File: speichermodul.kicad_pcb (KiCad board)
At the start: 2 copper layers, 100 x 160 mm, 66 parts, among them IC1 6116, P1 CONN_3X2, P2 CONN_01X01, P3 CONN_01X01, P4 CONN_01X01, P5 CONN_01X01, P6 CONN_01X01, P7 CONN_01X01, P8 CONN_02X10, P9 CONN_02X10, SW1 SW_PUSH, SW2 SW_PUSH, U1 7400, U2 74LS08, U3 74LS08, U4 74LS14, U5 74LS540, U6 74LS540

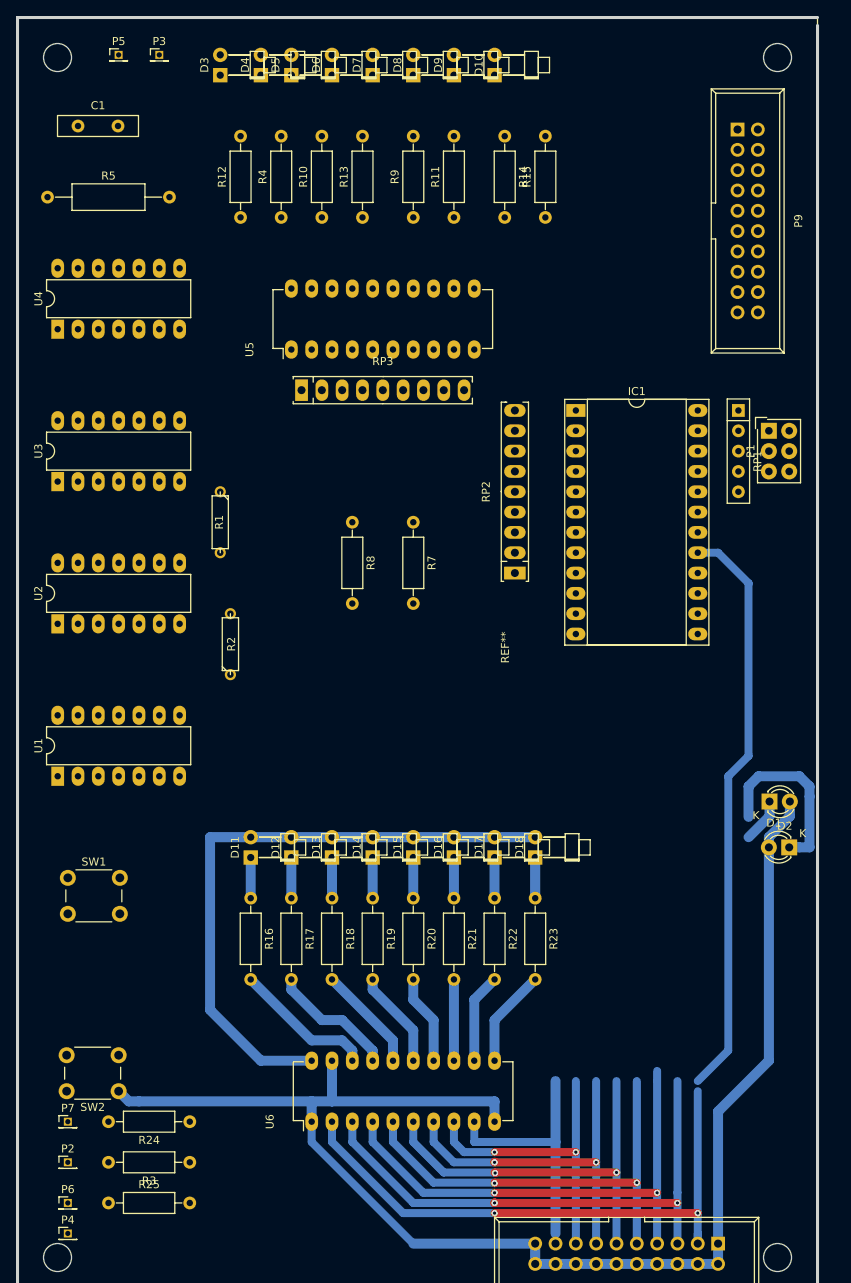
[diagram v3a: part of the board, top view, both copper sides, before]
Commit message: PCB layout revolutioniert
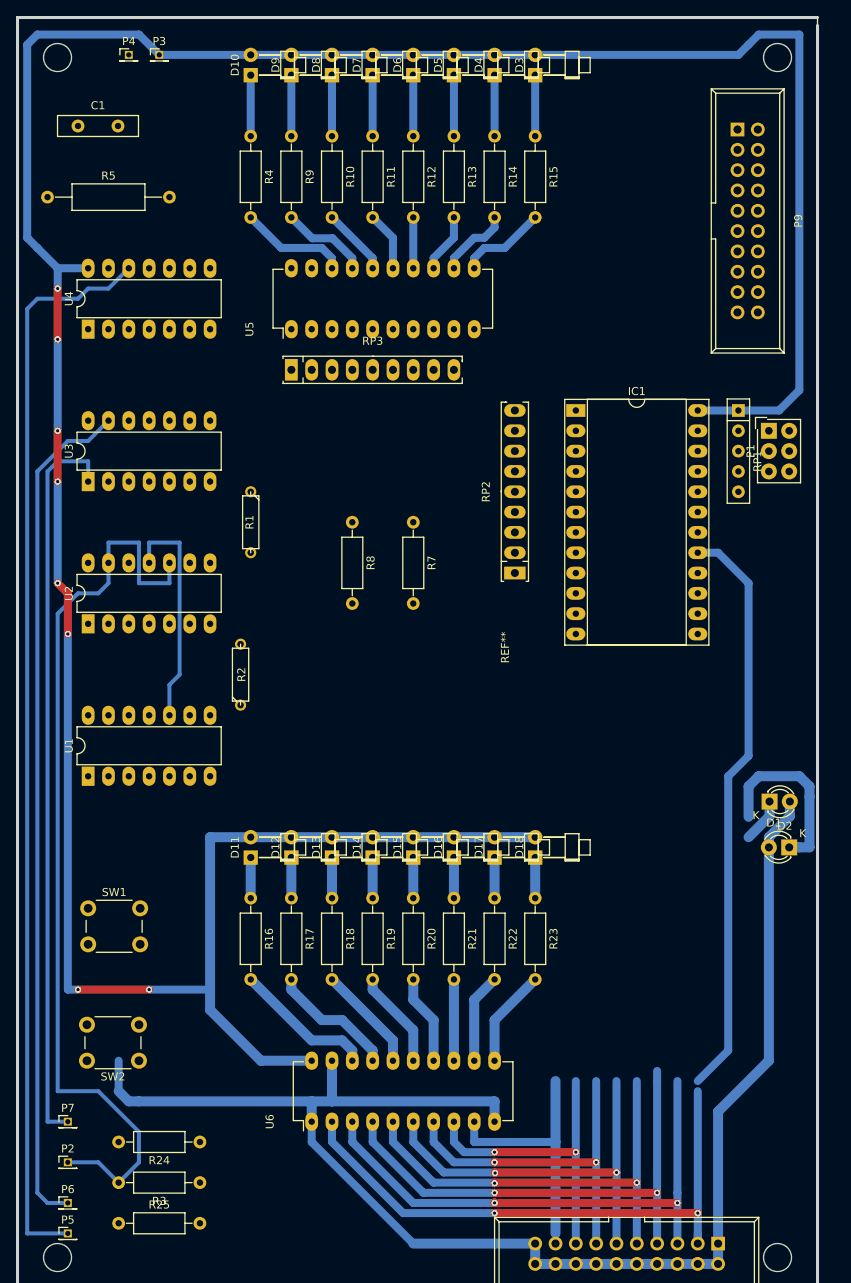
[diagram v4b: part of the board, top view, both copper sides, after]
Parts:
- moved P4 147.5 mm to (41.9, 26.7)
- moved P5 147.5 mm to (34.3, 174.0)
- moved D3 39.4 mm to (92.7, 29.2)
- moved D10 30.5 mm to (57.1, 29.2)
- moved D4 29.2 mm to (87.6, 29.2)
- moved R12 23.9 mm to (77.5, 36.8), turned to 270 degrees
- moved D5 20.3 mm to (82.5, 29.2)
- moved D9 20.3 mm to (62.2, 29.2)
- moved R9 18.3 mm to (62.2, 36.8), turned to 270 degrees
- moved R13 15.3 mm to (82.5, 36.8), turned to 270 degrees
- moved R11 14.4 mm to (72.4, 36.8), turned to 270 degrees
- moved R4 10.9 mm to (57.1, 36.8), turned to 270 degrees
- moved R15 10.2 mm to (92.7, 36.8), turned to 270 degrees
- moved R10 10.2 mm to (67.3, 36.8), turned to 270 degrees
- moved D6 10.2 mm to (77.5, 29.2)
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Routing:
- net VCC: track 77.6 -> 376.7 mm, vias 0 -> 8
- net Net-(P5-Pad1): track 0.00 -> 135.5 mm
- net /_auto: track 0.00 -> 115.0 mm
- net Net-(P6-Pad1): track 0.00 -> 106.0 mm
- net Net-(P7-Pad1): track 0.00 -> 92.0 mm
- net Net-(U1-Pad10): track 0.00 -> 28.5 mm
- net Net-(R4-Pad2): track 0.00 -> 13.5 mm
- net Net-(R9-Pad2): track 0.00 -> 11.0 mm
- net Net-(R15-Pad2): track 0.00 -> 11.0 mm
- net Net-(R14-Pad2): track 0.00 -> 9.20 mm
- net Net-(R10-Pad2): track 0.00 -> 8.45 mm
- net Net-(D9-Pad1): track 0.00 -> 7.62 mm
- net Net-(D8-Pad1): track 0.00 -> 7.62 mm
- net Net-(D7-Pad1): track 0.00 -> 7.62 mm
- net Net-(D6-Pad1): track 0.00 -> 7.62 mm
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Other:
- net class Default: trace_width 1 -> 0.5

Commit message: minimal änderungen
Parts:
- moved P8 139.7 mm to (118.1, 35.6), turned to 270 degrees
- moved P9 139.3 mm to (115.6, 175.3), turned to 180 degrees
- moved SW2 16.6 mm to (44.5, 135.9)
- moved SW1 15.2 mm to (36.8, 148.6)
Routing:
- net GND: track 184.1 -> 103.5 mm
- net /D7: track 72.8 -> 0.00 mm
- net Net-(U1-Pad5): track 0.00 -> 18.1 mm
- net /A2: track 62.3 -> 47.1 mm
- net /A1: track 66.8 -> 51.6 mm
- net /A0: track 72.3 -> 57.0 mm
- net /A3: track 55.5 -> 42.8 mm
- net /A4: track 49.9 -> 38.5 mm
- net VCC: track 376.7 -> 386.9 mm
- net /A5: track 44.4 -> 34.2 mm
- net /A6: track 38.6 -> 29.7 mm
- net Net-(U2-Pad6): track 0.00 -> 7.62 mm
- net Net-(U2-Pad12): track 0.00 -> 7.62 mm
- net /A7: track 31.8 -> 25.4 mm

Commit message: Nix
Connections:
- P9 pad 11: /D4 -> /D3
- P9 pad 13: /D5 -> /D2
- P9 pad 15: /D6 -> /D1
- P9 pad 17: /D7 -> /D0
- P9 pad 3: /D0 -> /D7
- P9 pad 5: /D1 -> /D6
- P9 pad 7: /D2 -> /D5
- P9 pad 9: /D3 -> /D4
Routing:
- net /A0: track 57.0 -> 26.5 mm, vias 2 -> 1
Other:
- net class Default: trace_width 0.5 -> 0.9
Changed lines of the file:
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@@
-(kicad_pcb (version 20171130) (host pcbnew no-vcs-found-bf44d39~61~ubuntu16.04.1)
+(kicad_pcb (version 20171130) (host pcbnew 5.0.0-rc2-dev-unknown-41ac458~64~ubuntu16.04.1)
   (general
     (thickness 1.6)
     (drawings 0)
-    (tracks 244)
+    (tracks 240)
     (zones 0)
     (modules 66)
@@
   )
   (setup
-    (last_trace_width 0.5)
+    (last_trace_width 0.9)
     (trace_clearance 0.2)
     (zone_clearance 0.508)
@@
   (net_class Default "This is the default net class."
     (clearance 0.2)
-    (trace_width 0.5)
+    (trace_width 0.9)
     (via_dia 0.8)
     (via_drill 0.4)
@@
       (net 10 GND))
     (pad 3 thru_hole oval (at 2.54 0 180) (size 1.7272 1.7272) (drill 1.016) (layers *.Cu *.Mask F.SilkS)
-      (net 2 /D0))
+      (net 9 /D7))
     (pad 4 thru_hole oval (at 2.54 -2.54 180) (size 1.7272 1.7272) (drill 1.016) (layers *.Cu *.Mask F.SilkS)
       (net 10 GND))
     (pad 5 thru_hole oval (at 5.08 0 180) (size 1.7272 1.7272) (drill 1.016) (layers *.Cu *.Mask F.SilkS)
-      (net 3 /D1))
+      (net 8 /D6))
     (pad 6 thru_hole oval (at 5.08 -2.54 180) (size 1.7272 1.7272) (drill 1.016) (layers *.Cu *.Mask F.SilkS)
       (net 10 GND))
     (pad 7 thru_hole oval (at 7.62 0 180) (size 1.7272 1.7272) (drill 1.016) (layers *.Cu *.Mask F.SilkS)
-      (net 4 /D2))
+      (net 7 /D5))
     (pad 8 thru_hole oval (at 7.62 -2.54 180) (size 1.7272 1.7272) (drill 1.016) (layers *.Cu *.Mask F.SilkS)
       (net 10 GND))
     (pad 9 thru_hole oval (at 10.16 0 180) (size 1.7272 1.7272) (drill 1.016) (layers *.Cu *.Mask F.SilkS)
-      (net 5 /D3))
+      (net 6 /D4))
     (pad 10 thru_hole oval (at 10.16 -2.54 180) (size 1.7272 1.7272) (drill 1.016) (layers *.Cu *.Mask F.SilkS)
       (net 10 GND))
     (pad 11 thru_hole oval (at 12.7 0 180) (size 1.7272 1.7272) (drill 1.016) (layers *.Cu *.Mask F.SilkS)
-      (net 6 /D4))
+      (net 5 /D3))
     (pad 12 thru_hole oval (at 12.7 -2.54 180) (size 1.7272 1.7272) (drill 1.016) (layers *.Cu *.Mask F.SilkS)
       (net 10 GND))
     (pad 13 thru_hole oval (at 15.24 0 180) (size 1.7272 1.7272) (drill 1.016) (layers *.Cu *.Mask F.SilkS)
-      (net 7 /D5))
+      (net 4 /D2))
     (pad 14 thru_hole oval (at 15.24 -2.54 180) (size 1.7272 1.7272) (drill 1.016) (layers *.Cu *.Mask F.SilkS)
       (net 10 GND))
     (pad 15 thru_hole oval (at 17.78 0 180) (size 1.7272 1.7272) (drill 1.016) (layers *.Cu *.Mask F.SilkS)
-      (net 8 /D6))
+      (net 3 /D1))
     (pad 16 thru_hole oval (at 17.78 -2.54 180) (size 1.7272 1.7272) (drill 1.016) (layers *.Cu *.Mask F.SilkS)
       (net 10 GND))
     (pad 17 thru_hole oval (at 20.32 0 180) (size 1.7272 1.7272) (drill 1.016) (layers *.Cu *.Mask F.SilkS)
-      (net 9 /D7))
+      (net 2 /D0))
     (pad 18 thru_hole oval (at 20.32 -2.54 180) (size 1.7272 1.7272) (drill 1.016) (layers *.Cu *.Mask F.SilkS)
       (net 10 GND))
@@
   (segment (start 69.85 162.56) (end 77.47 170.18) (width 1) (layer B.Cu) (net 33))
   (segment (start 87.63 170.18) (end 87.63 170.18) (width 1) (layer F.Cu) (net 33) (status 2))
-  (via (at 113.03 171.45) (size 0.8) (drill 0.4) (layers F.Cu B.Cu) (net 34))
-  (segment (start 67.31 162.56) (end 76.2 171.45) (width 1) (layer B.Cu) (net 34))
-  (segment (start 76.2 171.45) (end 87.63 171.45) (width 1) (layer B.Cu) (net 34))
-  (segment (start 67.31 160.02) (end 67.31 162.56) (width 1) (layer B.Cu) (net 34) (status 400000))
+  (segment (start 67.31 160.02) (end 67.31 162.56) (width 0.9) (layer B.Cu) (net 34))
+  (segment (start 67.31 162.56) (end 76.2 171.45) (width 0.9) (layer B.Cu) (net 34))
   (via (at 87.63 171.45) (size 0.8) (drill 0.4) (layers F.Cu B.Cu) (net 34))
-  (segment (start 87.63 171.45) (end 113.03 171.45) (width 1) (layer F.Cu) (net 34))
-  (segment (start 113.03 175.26) (end 113.03 171.45) (width 1) (layer B.Cu) (net 34) (status 400000))
-  (segment (start 113.03 175.26) (end 113.03 173.99) (width 1) (layer B.Cu) (net 34) (status 400000))
+  (segment (start 76.2 171.45) (end 87.63 171.45) (width 0.9) (layer B.Cu) (net 34))
   (segment (start 124.46 125.73) (end 125.73 125.73) (width 1.25) (layer B.Cu) (net 35) (status 400000))
   (segment (start 119.38 118.11) (end 119.38 121.92) (width 1.25) (layer B.Cu) (net 35))
@@
   (segment (start 62.23 36.83) (end 62.23 29.21) (width 1) (layer B.Cu) (net 68) (status C00000))
   (segment (start 57.15 36.83) (end 57.15 29.21) (width 1) (layer B.Cu) (net 69) (status C00000))
-  (segment (start 57.15 132.08) (end 57.15 127) (width 1.25) (layer B.Cu) (net 77) (status C00000))
-  (segment (start 62.23 132.08) (end 62.23 127) (width 1.25) (layer B.Cu) (net 76) (status C00000))
-  (segment (start 67.31 132.08) (end 67.31 127) (width 1.25) (layer B.Cu) (net 75) (status C00000))
-  (segment (start 72.39 132.08) (end 72.39 127) (width 1.25) (layer B.Cu) (net 74) (status C00000))
-  (segment (start 77.47 132.08) (end 77.47 127) (width 1.25) (layer B.Cu) (net 73) (status C00000))
-  (segment (start 82.55 132.08) (end 82.55 127) (width 1.25) (layer B.Cu) (net 72) (status C00000))
-  (segment (start 87.63 132.08) (end 87.63 127) (width 1.25) (layer B.Cu) (net 71) (status C00000))
   (segment (start 92.71 132.08) (end 92.71 127) (width 1.25) (layer B.Cu) (net 70) (status C00000))
+  (segment (start 87.63 132.08) (end 87.63 127) (width 1.25) (layer B.Cu) (net 71) (status C00000))
+  (segment (start 82.55 132.08) (end 82.55 127) (width 1.25) (layer B.Cu) (net 72) (status C00000))
+  (segment (start 77.47 132.08) (end 77.47 127) (width 1.25) (layer B.Cu) (net 73) (status C00000))
+  (segment (start 72.39 132.08) (end 72.39 127) (width 1.25) (layer B.Cu) (net 74) (status C00000))
+  (segment (start 67.31 132.08) (end 67.31 127) (width 1.25) (layer B.Cu) (net 75) (status C00000))
+  (segment (start 62.23 132.08) (end 62.23 127) (width 1.25) (layer B.Cu) (net 76) (status C00000))
+  (segment (start 57.15 132.08) (end 57.15 127) (width 1.25) (layer B.Cu) (net 77) (status C00000))
 )

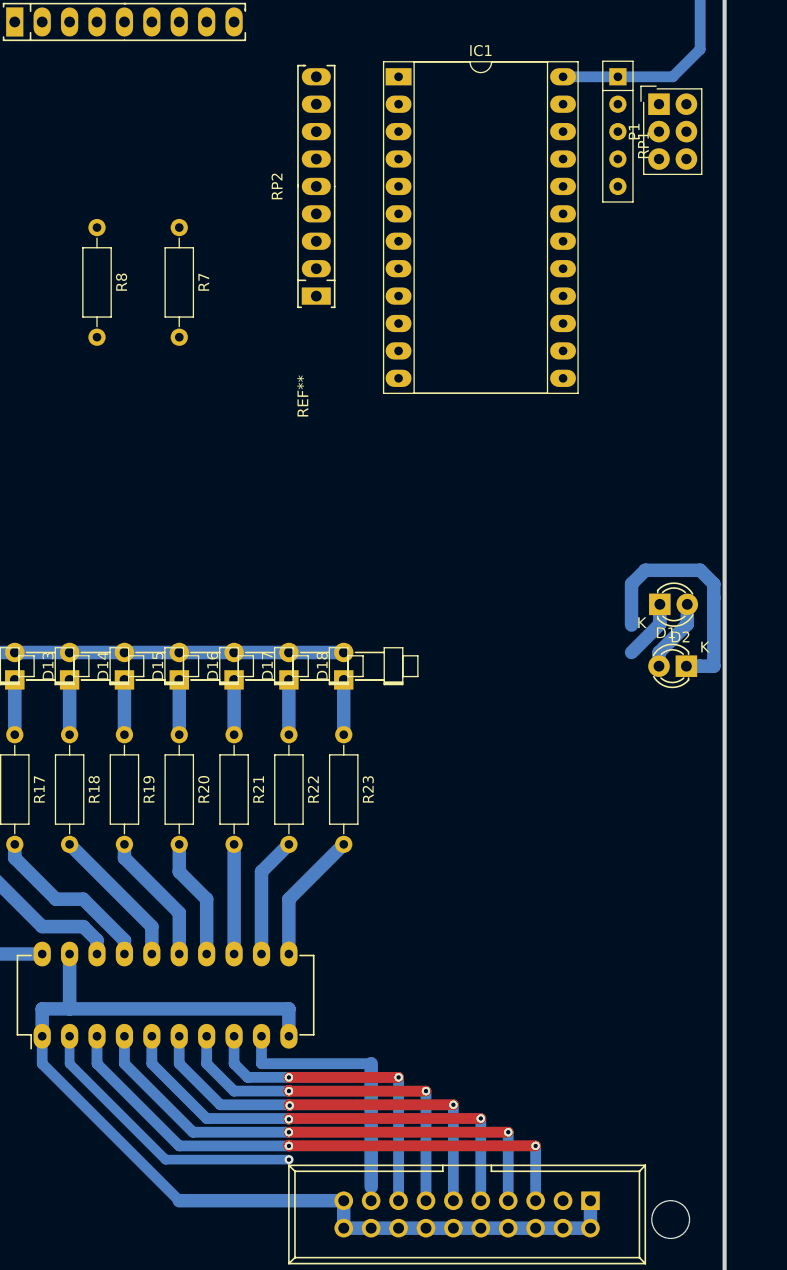
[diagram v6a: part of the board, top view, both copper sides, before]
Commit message: ein einzelnes footprint geändert
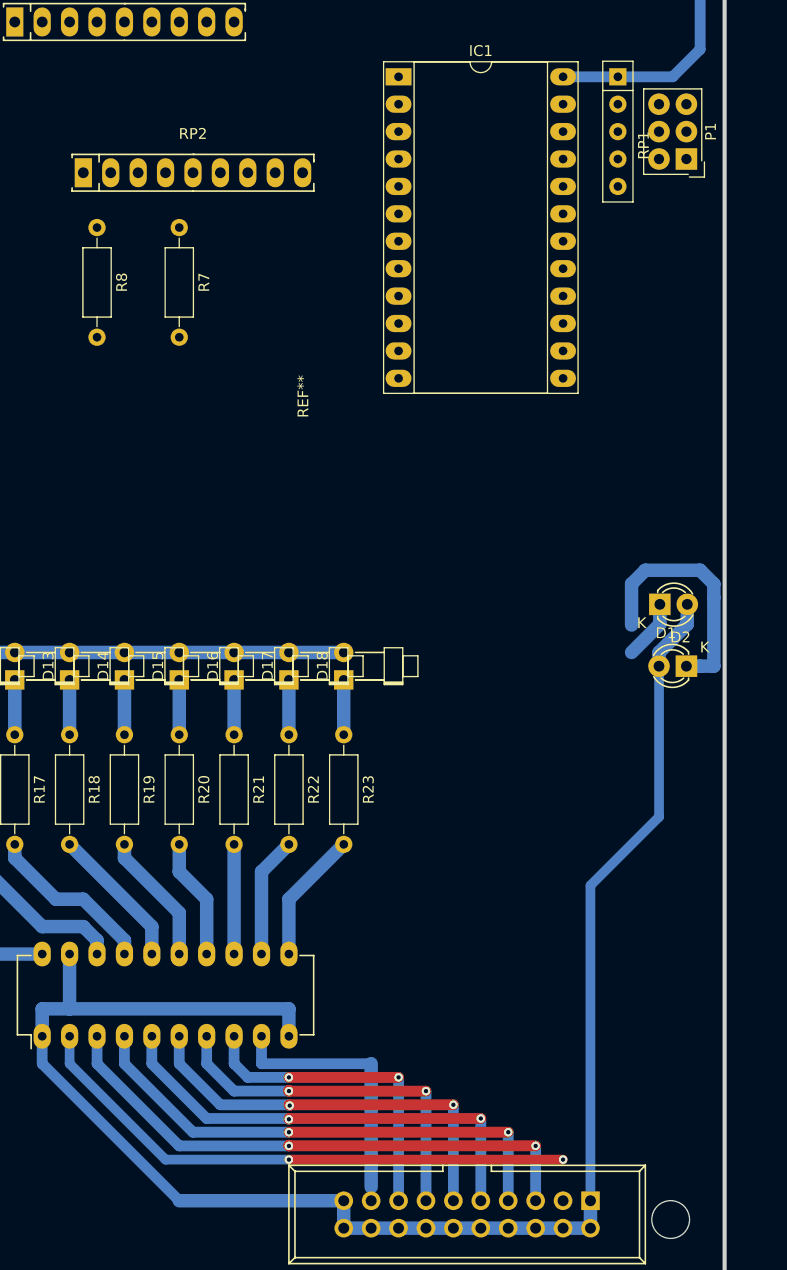
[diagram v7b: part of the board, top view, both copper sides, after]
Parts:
- moved RP2 11.5 mm to (78.7, 80.0), turned to 0 degrees
- moved P1 5.68 mm to (124.5, 78.7), turned to 180 degrees
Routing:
- net GND: track 103.5 -> 155.7 mm
- net /A0: track 26.5 -> 51.9 mm, vias 1 -> 2

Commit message: KAel verlegt
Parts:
- removed the REF** at (28.0, 22.0)
- removed RP2: R_PACK8BUSSED, Housings_SIP:SIP9_Housing_BigPads
- added REF**: EuroBoard160mmX100mm, EuroBoard_Outline:EuroBoard160mmX100mm, F.Cu at (128.3, 181.6)
- moved SW2 17.8 mm to (43.2, 153.7)
- moved SW1 15.2 mm to (36.8, 133.3)
- moved R1 1.27 mm to (58.4, 85.1)
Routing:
- net GND: track 155.7 -> 311.2 mm
- net /D7: track 0.00 -> 93.4 mm
- net /D0: track 0.00 -> 93.0 mm
- net /D6: track 0.00 -> 90.9 mm
- net /D1: track 0.00 -> 89.4 mm
- net /D5: track 0.00 -> 88.3 mm
- net /D4: track 0.00 -> 85.8 mm
- net /D2: track 0.00 -> 85.8 mm
- net /D3: track 0.00 -> 83.3 mm
- net VCC: track 386.9 -> 463.0 mm
- net /A0: track 51.9 -> 0.00 mm, vias 2 -> 0
- net /A1: track 51.6 -> 0.00 mm, vias 2 -> 0
- net /A2: track 47.1 -> 0.00 mm, vias 2 -> 0
- net /A3: track 42.8 -> 0.00 mm, vias 2 -> 0
- net /A4: track 38.5 -> 0.00 mm, vias 2 -> 0
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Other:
- outline, holes or cut-outs redrawn
- net class Default: trace_width 0.9 -> 0.8
